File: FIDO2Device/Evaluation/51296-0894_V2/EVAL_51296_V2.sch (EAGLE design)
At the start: 25 parts, among them CN1 51296-0894, CN2 IF_6PIN, CN3 IF_3PIN, CN4 IF_4PIN, Q1 BSS84AKQBZ, U1 RV-3028-C7

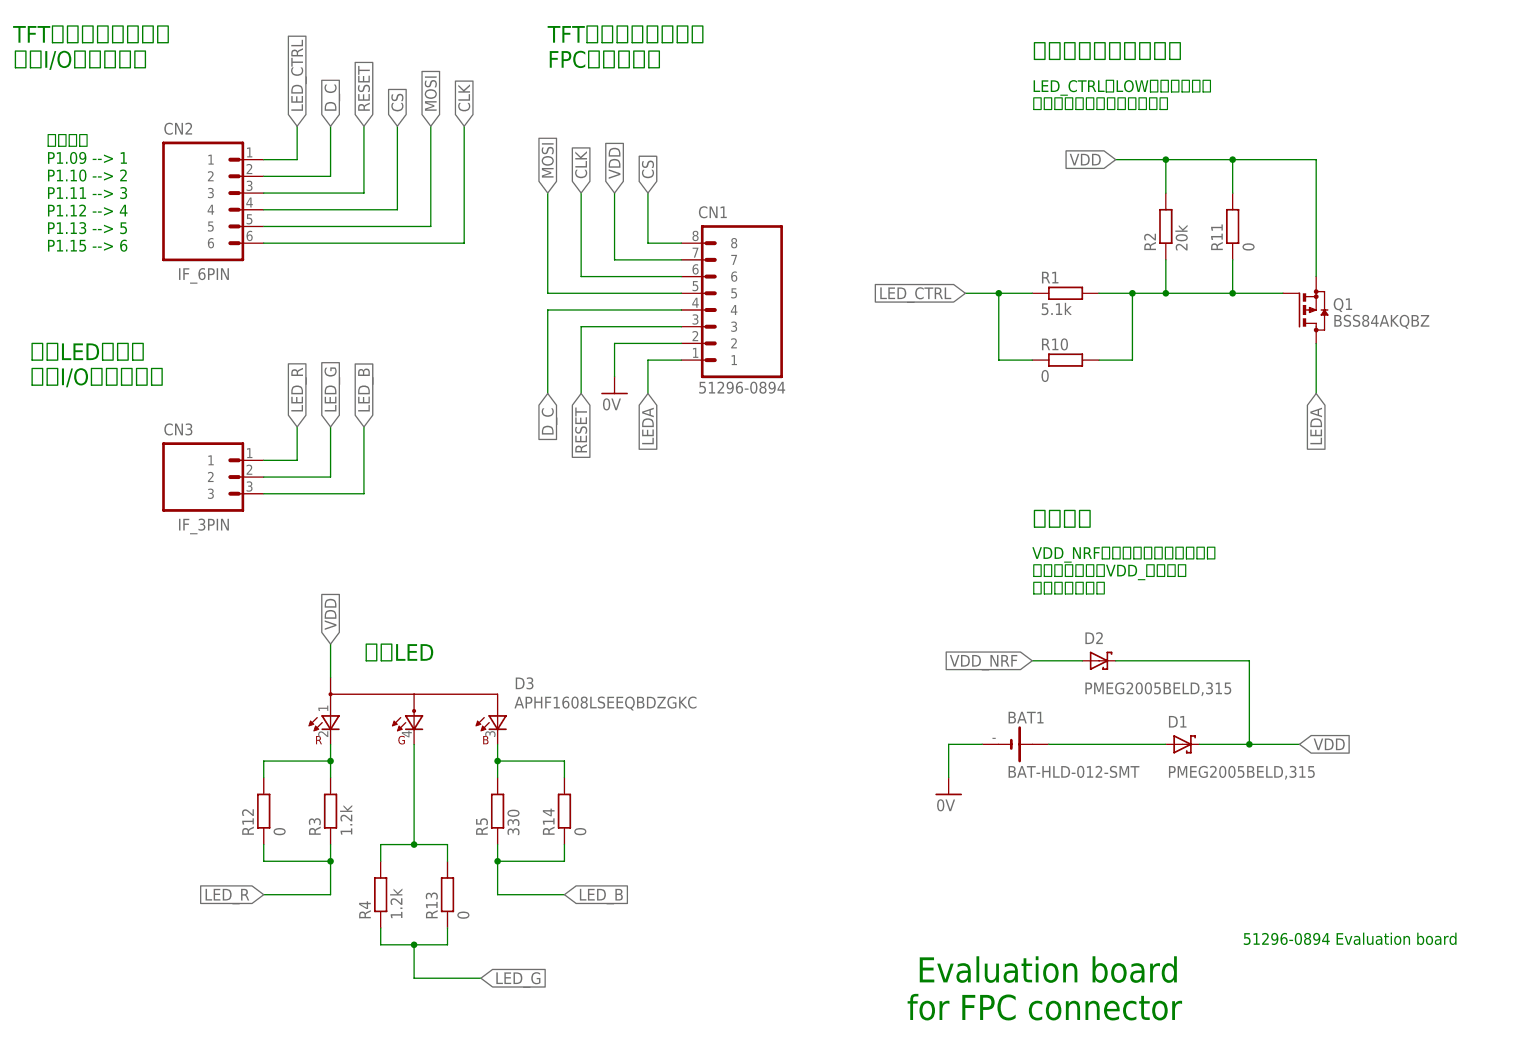
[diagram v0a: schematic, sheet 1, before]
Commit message: 回路図を修正
・MOSFETのゲート／ソースのピン番号が逆転していたので修正
・ジャンパー（R10〜R14）を実装しない旨明記
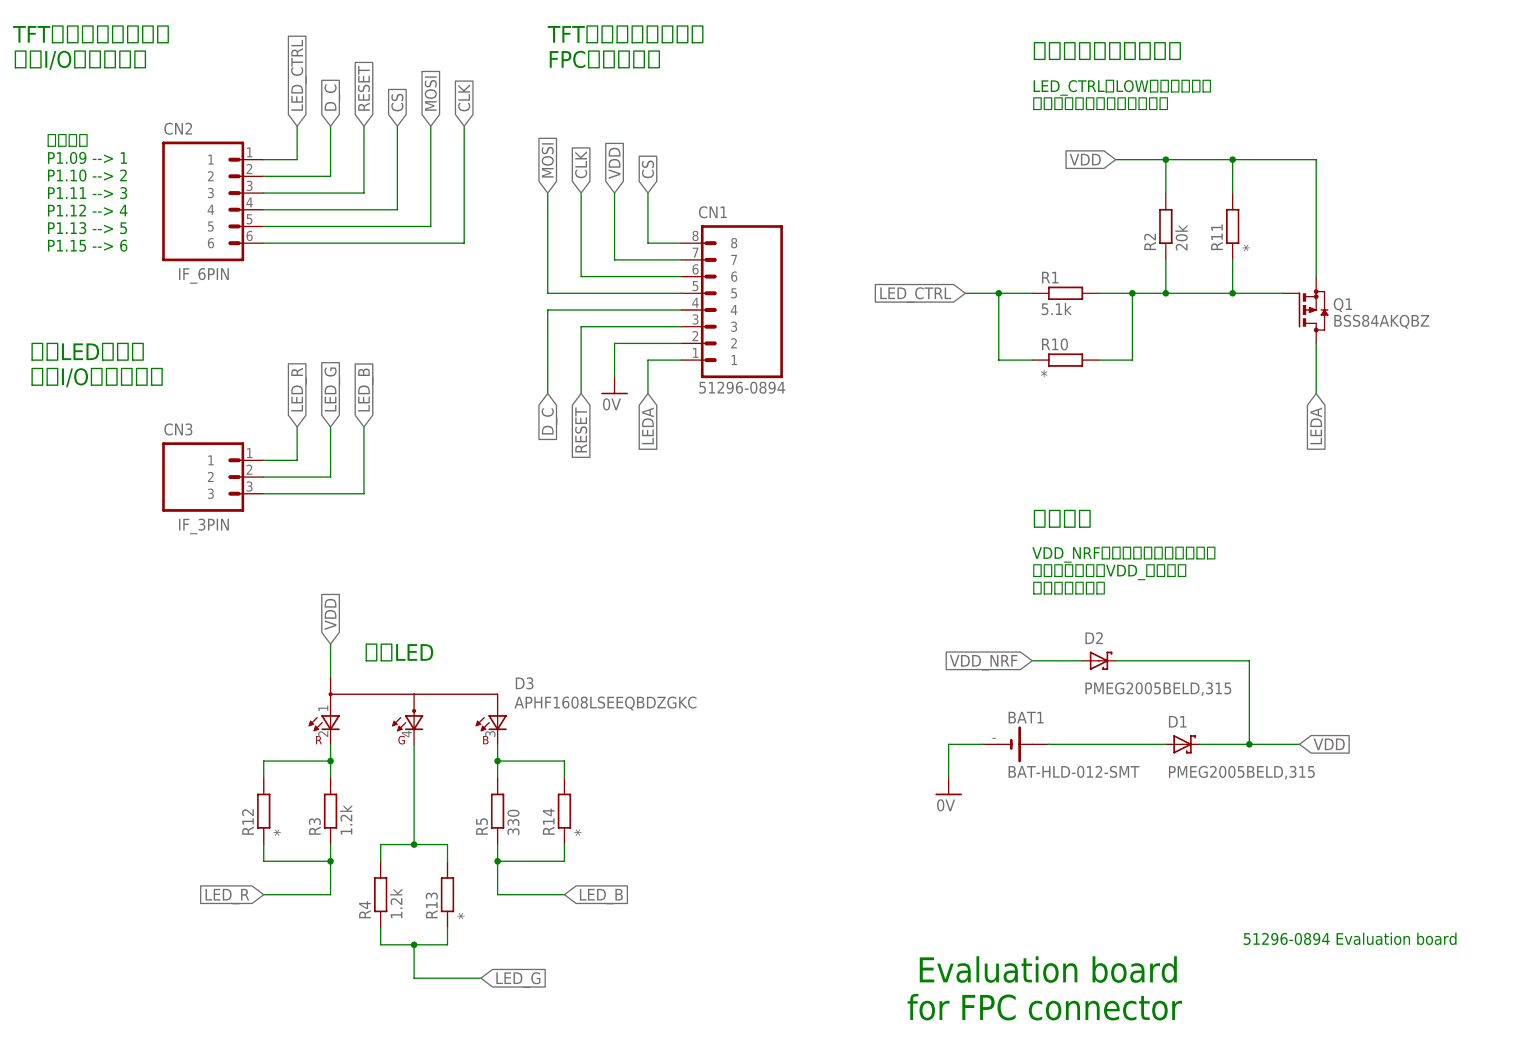
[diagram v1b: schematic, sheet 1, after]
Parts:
- R10, R11, R12, R13, R14: value 0 -> *
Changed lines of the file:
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@@
 <part name="R4" library="Parts" deviceset="RESISTOR" device="_0402N" value="1.2k"/>
 <part name="R5" library="Parts" deviceset="RESISTOR" device="_0402N" value="330"/>
-<part name="R10" library="Parts" deviceset="RESISTOR" device="_200MIL" value="0"/>
-<part name="R11" library="Parts" deviceset="RESISTOR" device="_200MIL" value="0"/>
-<part name="R12" library="Parts" deviceset="RESISTOR" device="_200MIL" value="0"/>
-<part name="R13" library="Parts" deviceset="RESISTOR" device="_200MIL" value="0"/>
-<part name="R14" library="Parts" deviceset="RESISTOR" device="_200MIL" value="0"/>
+<part name="R10" library="Parts" deviceset="RESISTOR" device="_200MIL" value="*"/>
+<part name="R11" library="Parts" deviceset="RESISTOR" device="_200MIL" value="*"/>
+<part name="R12" library="Parts" deviceset="RESISTOR" device="_200MIL" value="*"/>
+<part name="R13" library="Parts" deviceset="RESISTOR" device="_200MIL" value="*"/>
+<part name="R14" library="Parts" deviceset="RESISTOR" device="_200MIL" value="*"/>
 </parts>
 <sheets>
